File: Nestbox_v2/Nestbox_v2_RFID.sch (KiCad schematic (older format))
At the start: 6 parts, among them U401 MLX90109

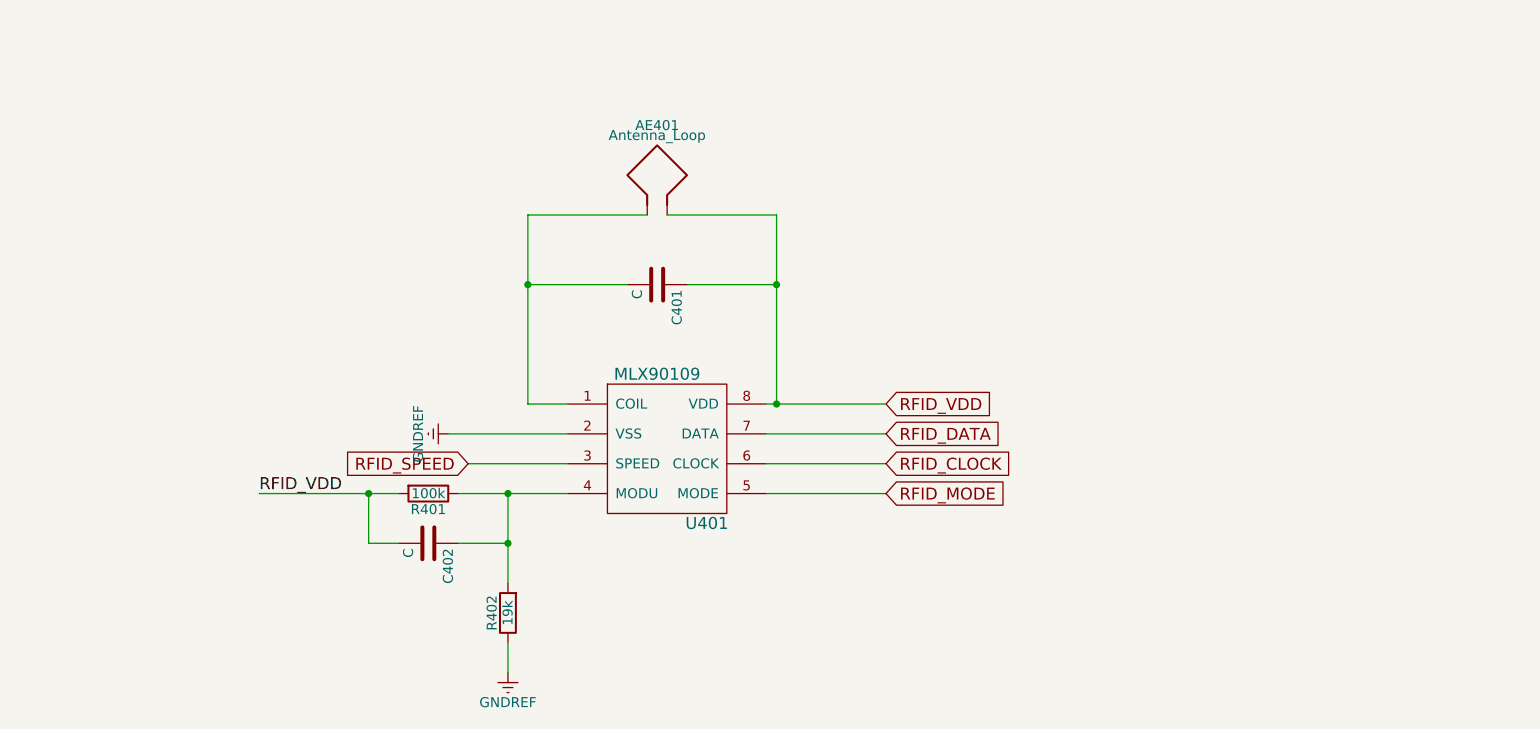
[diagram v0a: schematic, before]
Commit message: Modifies RFID circuit
- Correctly calculate resistive divider to get 0.9 V from 3.3
- Hardwire speed input
- Connect MODU to global label (to MSP430)
- Annotate schematic
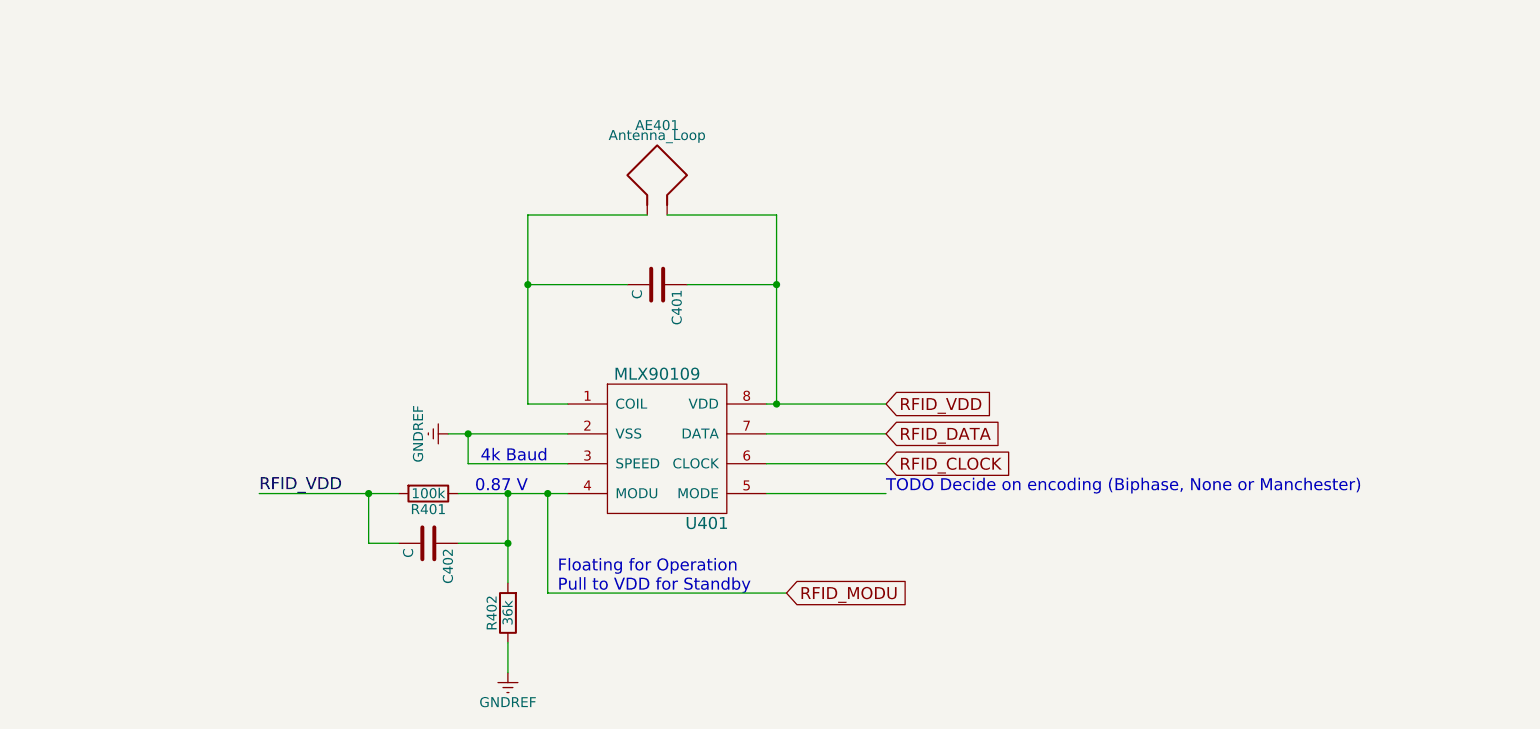
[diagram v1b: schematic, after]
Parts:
- R402: value 19k -> 36k
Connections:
- net labels added: RFID_MODU
- net labels removed: RFID_MODE, RFID_SPEED
- wire segments 20 -> 23
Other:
- note added: "0.87 V"
- note added: "4k Baud"
- note added: "Floating for Operation\nPull to VDD for Standby\n"
- note added: "TODO Decide on encoding (Biphase, None or Manchester)"
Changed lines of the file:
@@
 P 4500 4550
 F 0 "R402" V 4580 4550 50  0000 C CNN
-F 1 "19k" V 4500 4550 50  0000 C CNN
+F 1 "36k" V 4500 4550 50  0000 C CNN
 F 2 "" V 4430 4550 50  0001 C CNN
 F 3 "" H 4500 4550 50  0001 C CNN
@@
 $EndComp
 Wire Wire Line
-	3950 3950 3250 3950
+	3250 3950 3950 3950
 Text Label 3250 3950 0    60   ~ 0
 RFID_VDD
@@
 Text GLabel 6400 3800 2    60   Input ~ 0
 RFID_CLOCK
-Text GLabel 6400 3950 2    60   Input ~ 0
-RFID_MODE
-Text GLabel 4300 3800 0    60   Input ~ 0
-RFID_SPEED
+Wire Wire Line
+	4300 3800 4300 3650
+Connection ~ 4300 3650
+Text Notes 4700 3800 2    60   ~ 0
+4k Baud
+Wire Wire Line
+	4700 3950 4700 4450
+Wire Wire Line
+	4700 4450 5900 4450
+Connection ~ 4700 3950
+Text GLabel 5900 4450 2    60   Input ~ 0
+RFID_MODU
+Text Notes 4750 4450 0    60   ~ 0
+Floating for Operation\nPull to VDD for Standby\n
+Text Notes 6400 3950 0    60   ~ 0
+TODO Decide on encoding (Biphase, None or Manchester)
+Text Notes 4600 3950 2    60   ~ 0
+0.87 V
 $EndSCHEMATC

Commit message: Changes MODU connection for RFID
- MODU connection was changed to be low end of R divider
- Added additional C in parallel with antenna, to allow more exact C setting
and have SMD as well as THT C available
- Added 0Ohm in VDD connection to be able to disconnect RFID if needed
- Annotated elements
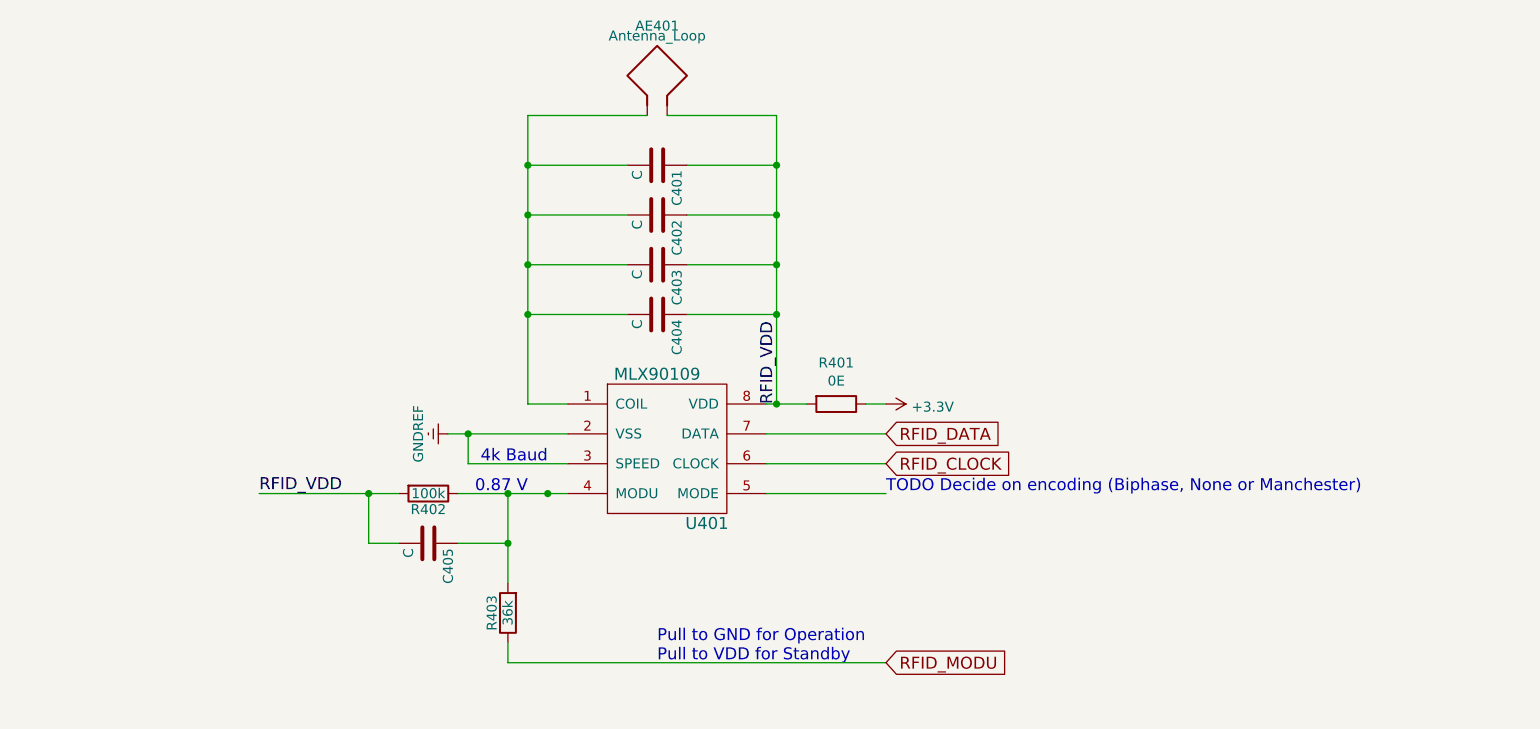
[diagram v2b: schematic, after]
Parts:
- added C401, C402, C403: C, symbol C
- added R401: 0E, symbol R
- renumbered C401 to C404, C402 to C405, R401 to R402, R402 to R403
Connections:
- net labels added: +3.3V
- wire segments 23 -> 29
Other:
- note added: "Pull to GND for Operation\nPull to VDD for Standby\n"
- note removed: "Floating for Operation\nPull to VDD for Standby\n"
- moved on the sheet: AE401, C404
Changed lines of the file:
@@
 $EndComp
 Wire Wire Line
-	5800 3500 6400 3500
+	5800 3500 6000 3500
 Wire Wire Line
 	5800 3650 6400 3650
@@
 	5800 3950 6400 3950
 $Comp
-L GNDREF #PWR401
+L GNDREF #PWR402
 U 1 1 59EF8071
 P 4200 3650
-F 0 "#PWR401" H 4200 3400 50  0001 C CNN
+F 0 "#PWR402" H 4200 3400 50  0001 C CNN
 F 1 "GNDREF" H 4200 3500 50  0000 C CNN
 F 2 "" H 4200 3650 50  0001 C CNN
@@
 	4200 3650 4800 3650
 $Comp
-L R R402
+L R R403
 U 1 1 59EF80B5
 P 4500 4550
-F 0 "R402" V 4580 4550 50  0000 C CNN
+F 0 "R403" V 4580 4550 50  0000 C CNN
 F 1 "36k" V 4500 4550 50  0000 C CNN
 F 2 "" V 4430 4550 50  0001 C CNN
@@
 $EndComp
 $Comp
-L R R401
+L R R402
 U 1 1 59EF815C
 P 4100 3950
-F 0 "R401" V 4180 3950 50  0000 C CNN
+F 0 "R402" V 4180 3950 50  0000 C CNN
 F 1 "100k" V 4100 3950 50  0000 C CNN
 F 2 "" V 4030 3950 50  0001 C CNN
@@
 Connection ~ 4500 3950
 Wire Wire Line
-	4500 4700 4500 4850
-$Comp
-L GNDREF #PWR402
-U 1 1 59EF81AA
-P 4500 4850
-F 0 "#PWR402" H 4500 4600 50  0001 C CNN
-F 1 "GNDREF" H 4500 4700 50  0000 C CNN
-F 2 "" H 4500 4850 50  0001 C CNN
-F 3 "" H 4500 4850 50  0001 C CNN
-	1    4500 4850
-	1    0    0    -1
-$EndComp
-Wire Wire Line
 	3250 3950 3950 3950
 Text Label 3250 3950 0    60   ~ 0
@@
 	4800 3800 4300 3800
 $Comp
-L C C401
+L C C404
 U 1 1 59EF8255
-P 5250 2900
-F 0 "C401" H 5275 3000 50  0000 L CNN
-F 1 "C" H 5275 2800 50  0000 L CNN
-F 2 "" H 5288 2750 50  0001 C CNN
-F 3 "" H 5250 2900 50  0001 C CNN
-	1    5250 2900
+P 5250 3050
+F 0 "C404" H 5275 3150 50  0000 L CNN
+F 1 "C" H 5275 2950 50  0000 L CNN
+F 2 "" H 5288 2900 50  0001 C CNN
+F 3 "" H 5250 3050 50  0001 C CNN
+	1    5250 3050
 	0    1    1    0
 $EndComp
@@
 	4600 3500 4800 3500
 Wire Wire Line
-	4600 2550 4600 3500
-Wire Wire Line
-	4600 2900 5100 2900
-Wire Wire Line
-	5400 2900 5850 2900
-Wire Wire Line
-	5850 2550 5850 3500
+	4600 3050 5100 3050
+Wire Wire Line
+	5850 3050 5400 3050
+Wire Wire Line
+	5850 2050 5850 3500
 Connection ~ 5850 3500
 $Comp
 L Antenna_Loop AE401
 U 1 1 59EF8372
-P 5200 2350
-F 0 "AE401" H 5250 2600 50  0000 C CNN
-F 1 "Antenna_Loop" H 5250 2550 50  0000 C CNN
-F 2 "" H 5200 2350 50  0001 C CNN
-F 3 "" H 5200 2350 50  0001 C CNN
-	1    5200 2350
+P 5200 1850
+F 0 "AE401" H 5250 2100 50  0000 C CNN
+F 1 "Antenna_Loop" H 5250 2050 50  0000 C CNN
+F 2 "" H 5200 1850 50  0001 C CNN
+F 3 "" H 5200 1850 50  0001 C CNN
+	1    5200 1850
 	1    0    0    -1
 $EndComp
 Wire Wire Line
-	4600 2550 5200 2550
-Connection ~ 4600 2900
-Wire Wire Line
-	5300 2550 5850 2550
-Connection ~ 5850 2900
+	4600 2050 5200 2050
+Connection ~ 4600 3050
+Wire Wire Line
+	5300 2050 5850 2050
+Connection ~ 5850 3050
 Wire Wire Line
 	4500 3950 4500 4400
 $Comp
-L C C402
+L C C405
 U 1 1 59EF857A
 P 4100 4200
-F 0 "C402" H 4125 4300 50  0000 L CNN
+F 0 "C405" H 4125 4300 50  0000 L CNN
 F 1 "C" H 4125 4100 50  0000 L CNN
 F 2 "" H 4138 4050 50  0001 C CNN
@@
 	4500 4200 4250 4200
 Connection ~ 4500 4200
-Text GLabel 6400 3500 2    60   Input ~ 0
-RFID_VDD
 Text GLabel 6400 3650 2    60   Input ~ 0
 RFID_DATA
@@
 4k Baud
 Wire Wire Line
-	4700 3950 4700 4450
-Wire Wire Line
-	4700 4450 5900 4450
+	4500 4800 6400 4800
 Connection ~ 4700 3950
-Text GLabel 5900 4450 2    60   Input ~ 0
+Text GLabel 6400 4800 2    60   Input ~ 0
 RFID_MODU
-Text Notes 4750 4450 0    60   ~ 0
-Floating for Operation\nPull to VDD for Standby\n
+Text Notes 5250 4800 0    60   ~ 0
+Pull to GND for Operation\nPull to VDD for Standby\n
 Text Notes 6400 3950 0    60   ~ 0
 TODO Decide on encoding (Biphase, None or Manchester)
 Text Notes 4600 3950 2    60   ~ 0
 0.87 V
+Wire Wire Line
+	4500 4700 4500 4800
+$Comp
+L C C403
+U 1 1 59FF2E8B
+P 5250 2800
+F 0 "C403" H 5275 2900 50  0000 L CNN
+F 1 "C" H 5275 2700 50  0000 L CNN
+F 2 "" H 5288 2650 50  0001 C CNN
+F 3 "" H 5250 2800 50  0001 C CNN
+	1    5250 2800
+	0    1    1    0
+$EndComp
+$Comp
+L C C402
+U 1 1 59FF2EB3
+P 5250 2550
+F 0 "C402" H 5275 2650 50  0000 L CNN
+F 1 "C" H 5275 2450 50  0000 L CNN
+F 2 "" H 5288 2400 50  0001 C CNN
+F 3 "" H 5250 2550 50  0001 C CNN
+	1    5250 2550
+	0    1    1    0
+$EndComp
+Wire Wire Line
+	4600 2800 5100 2800
+Connection ~ 4600 2800
+Connection ~ 4600 2550
+Wire Wire Line
+	4600 2050 4600 3500
+Wire Wire Line
+	4600 2550 5100 2550
+Wire Wire Line
+	5400 2550 5850 2550
+Connection ~ 5850 2550
+Wire Wire Line
+	5400 2800 5850 2800
+Connection ~ 5850 2800
+$Comp
+L C C401
+U 1 1 59FF305A
+P 5250 2300
+F 0 "C401" H 5275 2400 50  0000 L CNN
+F 1 "C" H 5275 2200 50  0000 L CNN
+F 2 "" H 5288 2150 50  0001 C CNN
+F 3 "" H 5250 2300 50  0001 C CNN
+	1    5250 2300
+	0    1    1    0
+$EndComp
+Wire Wire Line
+	4600 2300 5100 2300
+Connection ~ 4600 2300
+Wire Wire Line
+	5400 2300 5850 2300
+Connection ~ 5850 2300
+$Comp
+L R R401
+U 1 1 59FF3558
+P 6150 3500
+F 0 "R401" V 5943 3500 50  0000 C CNN
+F 1 "0E" V 6034 3500 50  0000 C CNN
+F 2 "" V 6080 3500 50  0000 C CNN
+F 3 "" H 6150 3500 50  0000 C CNN
+	1    6150 3500
+	0    1    1    0
+$EndComp
+$Comp
+L +3.3V #PWR401
+U 1 1 59FF36B1
+P 6400 3500
+F 0 "#PWR401" H 6400 3350 50  0001 C CNN
+F 1 "+3.3V" V 6415 3628 50  0000 L CNN
+F 2 "" H 6400 3500 50  0000 C CNN
+F 3 "" H 6400 3500 50  0000 C CNN
+	1    6400 3500
+	0    1    1    0
+$EndComp
+Wire Wire Line
+	6400 3500 6300 3500
+Text Label 5850 3500 1    60   ~ 0
+RFID_VDD
 $EndSCHEMATC

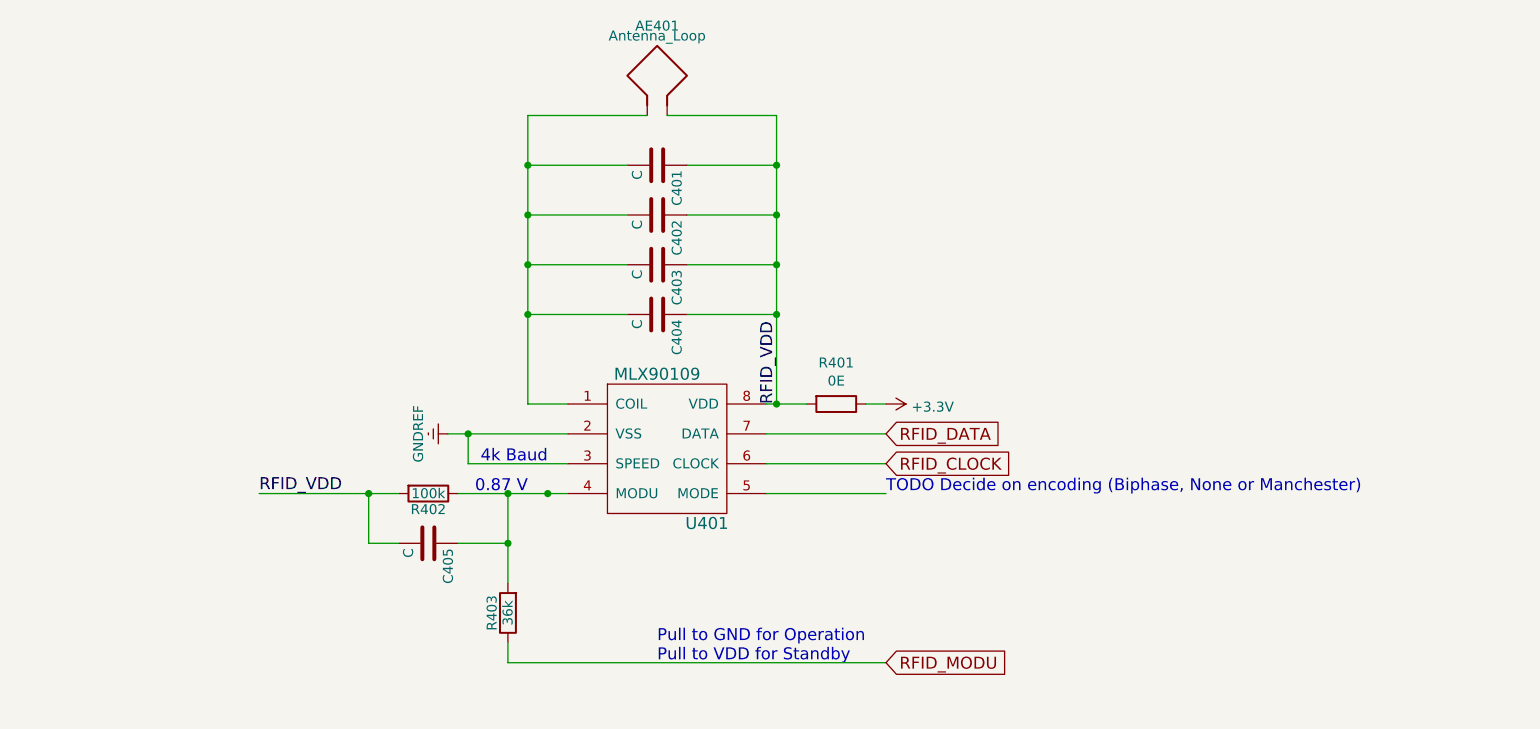
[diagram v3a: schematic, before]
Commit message: VDD select jumper added to RFID part
The VDD for the RFID chip can now be chosen between 5V and 3.3V using a
jumper.
TODO: Check the correct voltage levels for the MODU pin.
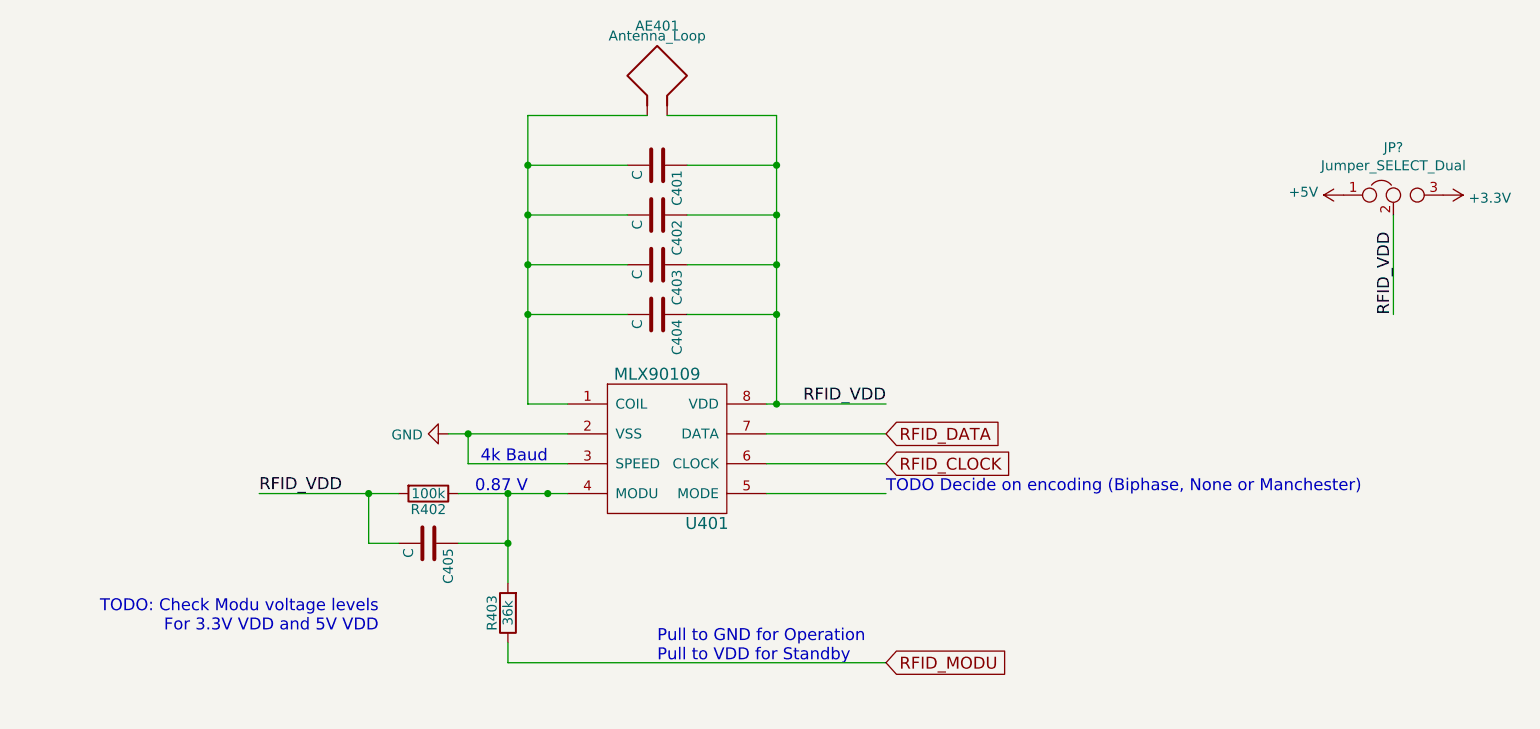
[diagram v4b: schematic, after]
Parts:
- removed R401: 0E, symbol R
- added JP?: Jumper_SELECT_Dual, symbol Jumper_SELECT_Dual
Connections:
- net +3V3: now also JP?.3
- net RFID_VDD: now also JP?.2
- net GNDREF renamed GND
- new net +5V: JP?.1
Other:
- note added: "TODO: Check Modu voltage levels\nFor 3.3V VDD and 5V VDD"
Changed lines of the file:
@@
 $EndComp
 Wire Wire Line
-	5800 3500 6000 3500
+	5800 3500 6400 3500
 Wire Wire Line
 	5800 3650 6400 3650
@@
 Wire Wire Line
 	5800 3950 6400 3950
-$Comp
-L GNDREF #PWR402
-U 1 1 59EF8071
-P 4200 3650
-F 0 "#PWR402" H 4200 3400 50  0001 C CNN
-F 1 "GNDREF" H 4200 3500 50  0000 C CNN
-F 2 "" H 4200 3650 50  0001 C CNN
-F 3 "" H 4200 3650 50  0001 C CNN
-	1    4200 3650
-	0    1    1    0
-$EndComp
 Wire Wire Line
 	4200 3650 4800 3650
@@
 Connection ~ 5850 2300
 $Comp
-L R R401
-U 1 1 59FF3558
-P 6150 3500
-F 0 "R401" V 5943 3500 50  0000 C CNN
-F 1 "0E" V 6034 3500 50  0000 C CNN
-F 2 "" V 6080 3500 50  0000 C CNN
-F 3 "" H 6150 3500 50  0000 C CNN
-	1    6150 3500
-	0    1    1    0
-$EndComp
-$Comp
 L +3.3V #PWR401
 U 1 1 59FF36B1
-P 6400 3500
-F 0 "#PWR401" H 6400 3350 50  0001 C CNN
-F 1 "+3.3V" V 6415 3628 50  0000 L CNN
-F 2 "" H 6400 3500 50  0000 C CNN
-F 3 "" H 6400 3500 50  0000 C CNN
-	1    6400 3500
-	0    1    1    0
-$EndComp
-Wire Wire Line
-	6400 3500 6300 3500
-Text Label 5850 3500 1    60   ~ 0
+P 9200 2450
+F 0 "#PWR401" H 9200 2300 50  0001 C CNN
+F 1 "+3.3V" V 9215 2578 50  0000 L CNN
+F 2 "" H 9200 2450 50  0000 C CNN
+F 3 "" H 9200 2450 50  0000 C CNN
+	1    9200 2450
+	0    1    1    0
+$EndComp
+Text Label 6400 3500 2    60   ~ 0
 RFID_VDD
+$Comp
+L Jumper_SELECT_Dual JP?
+U 1 1 5A0303B0
+P 8950 2450
+F 0 "JP?" H 8950 2689 50  0000 C CNN
+F 1 "Jumper_SELECT_Dual" H 8950 2598 50  0000 C CNN
+F 2 "" H 8950 2450 50  0001 C CNN
+F 3 "" H 8950 2450 50  0001 C CNN
+	1    8950 2450
+	1    0    0    -1
+$EndComp
+Wire Wire Line
+	8950 2550 8950 3050
+Text Label 8950 3050 1    60   ~ 0
+RFID_VDD
+$Comp
+L +5V #PWR?
+U 1 1 5A0305A8
+P 8700 2450
+F 0 "#PWR?" H 8700 2300 50  0001 C CNN
+F 1 "+5V" V 8715 2578 50  0000 L CNN
+F 2 "" H 8700 2450 50  0001 C CNN
+F 3 "" H 8700 2450 50  0001 C CNN
+	1    8700 2450
+	0    -1   -1   0
+$EndComp
+Text Notes 3850 4650 2    60   ~ 0
+TODO: Check Modu voltage levels\nFor 3.3V VDD and 5V VDD
+$Comp
+L GND #PWR?
+U 1 1 5A0312F4
+P 4200 3650
+F 0 "#PWR?" H 4200 3400 50  0001 C CNN
+F 1 "GND" V 4205 3522 50  0000 R CNN
+F 2 "" H 4200 3650 50  0001 C CNN
+F 3 "" H 4200 3650 50  0001 C CNN
+	1    4200 3650
+	0    1    1    0
+$EndComp
 $EndSCHEMATC
